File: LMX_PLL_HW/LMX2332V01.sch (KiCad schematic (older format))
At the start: 50 parts, among them J1 Conn_Coaxial, J2 Conn_01x04_Male, J3 Screw_Terminal_01x02, U1 Z-CommV440, U2 LMX2332, U3 ToyocomTCXO, U4 TPS784-Q1, U5 TPS784-Q1

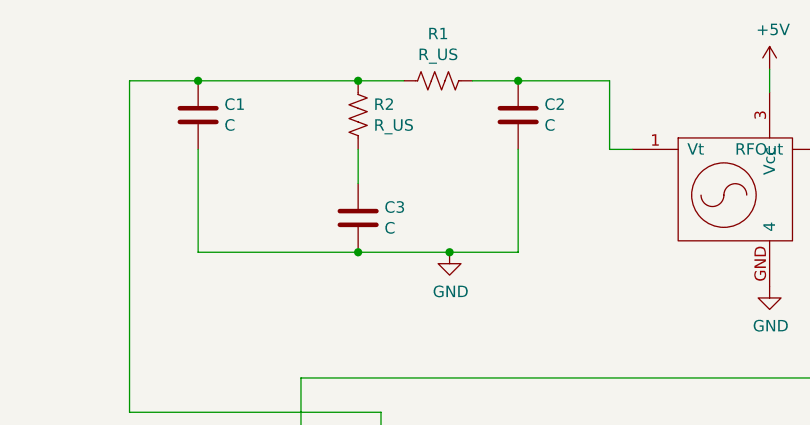
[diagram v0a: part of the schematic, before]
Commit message: Update 2021-07-05
Finished Schematic enough to get a first cut pulled into the layout.

Also finished PLL_Calculations.py enought to get loop filter component footprints nailed. Still needs more work, but ongoing. I'm using Spyder as a Python IDE.
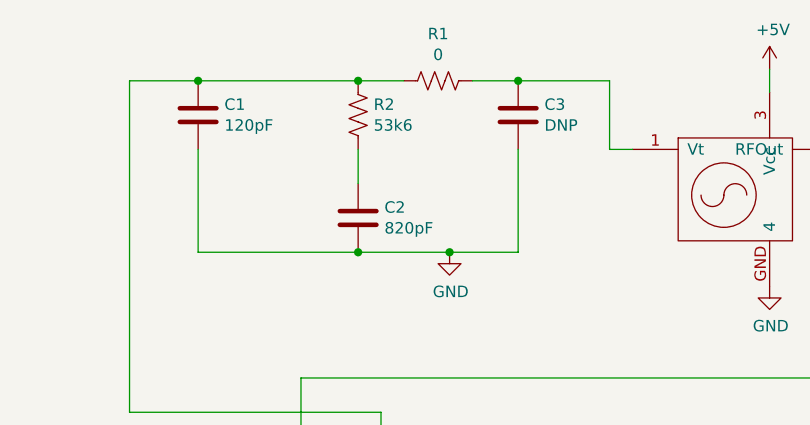
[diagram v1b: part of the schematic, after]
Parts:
- C1: value C -> 120pF; footprint (none) -> Capacitors_SMD:C_0805_HandSoldering
- C2: renamed from C3; value C -> 820pF; footprint (none) -> Capacitors_SMD:C_0805_HandSoldering
- C3: renamed from C2; value C -> DNP; footprint (none) -> Capacitors_SMD:C_0805_HandSoldering
- FB1: footprint (none) -> Capacitors_SMD:C_0805_HandSoldering
- J2: footprint (none) -> Connector_PinHeader_2.54mm:PinHeader_1x04_P2.54mm_Vertical
- J3: footprint (none) -> TerminalBlock_TE-Connectivity:TerminalBlock_TE_282834-2_1x02_P2.54mm_Horizontal
- R1: value R_US -> 0
- R2: value R_US -> 53k6
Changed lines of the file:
@@
 P 1950 1150
 F 0 "C1" H 2065 1196 50  0000 L CNN
-F 1 "C" H 2065 1105 50  0000 L CNN
-F 2 "" H 1988 1000 50  0001 C CNN
+F 1 "120pF" H 2065 1105 50  0000 L CNN
+F 2 "Capacitors_SMD:C_0805_HandSoldering" H 1988 1000 50  0001 C CNN
 F 3 "~" H 1950 1150 50  0001 C CNN
 	1    1950 1150
@@
 $EndComp
 $Comp
-L Device:C C3
+L Device:C C2
 U 1 1 60A5CF1C
 P 2650 1600
-F 0 "C3" H 2765 1646 50  0000 L CNN
-F 1 "C" H 2765 1555 50  0000 L CNN
-F 2 "" H 2688 1450 50  0001 C CNN
+F 0 "C2" H 2765 1646 50  0000 L CNN
+F 1 "820pF" H 2765 1555 50  0000 L CNN
+F 2 "Capacitors_SMD:C_0805_HandSoldering" H 2688 1450 50  0001 C CNN
 F 3 "~" H 2650 1600 50  0001 C CNN
 	1    2650 1600
@@
 $EndComp
 $Comp
-L Device:C C2
+L Device:C C3
 U 1 1 60A5D54A
 P 3350 1150
-F 0 "C2" H 3465 1196 50  0000 L CNN
-F 1 "C" H 3465 1105 50  0000 L CNN
-F 2 "" H 3388 1000 50  0001 C CNN
+F 0 "C3" H 3465 1196 50  0000 L CNN
+F 1 "DNP" H 3465 1105 50  0000 L CNN
+F 2 "Capacitors_SMD:C_0805_HandSoldering" H 3388 1000 50  0001 C CNN
 F 3 "~" H 3350 1150 50  0001 C CNN
 	1    3350 1150
@@
 P 2650 1150
 F 0 "R2" H 2718 1196 50  0000 L CNN
-F 1 "R_US" H 2718 1105 50  0000 L CNN
+F 1 "53k6" H 2718 1105 50  0000 L CNN
 F 2 "Resistors_SMD:R_0805_HandSoldering" V 2690 1140 50  0001 C CNN
 F 3 "~" H 2650 1150 50  0001 C CNN
@@
 P 3000 1000
 F 0 "R1" V 2795 1000 50  0000 C CNN
-F 1 "R_US" V 2886 1000 50  0000 C CNN
+F 1 "0" V 2886 1000 50  0000 C CNN
 F 2 "Resistors_SMD:R_0805_HandSoldering" V 3040 990 50  0001 C CNN
 F 3 "~" H 3000 1000 50  0001 C CNN
@@
 F 0 "J3" H 1118 9267 50  0000 C CNN
 F 1 "Screw_Terminal_01x02" H 1150 8850 50  0000 C CNN
-F 2 "" H 1200 9050 50  0001 C CNN
+F 2 "TerminalBlock_TE-Connectivity:TerminalBlock_TE_282834-2_1x02_P2.54mm_Horizontal" H 1200 9050 50  0001 C CNN
 F 3 "~" H 1200 9050 50  0001 C CNN
 	1    1200 9050
@@
 F 0 "FB1" V 1263 9050 50  0000 C CNN
 F 1 "Ferrite_Bead_Small" V 1350 9350 50  0000 C CNN
-F 2 "" V 1430 9050 50  0001 C CNN
+F 2 "Capacitors_SMD:C_0805_HandSoldering" V 1430 9050 50  0001 C CNN
 F 3 "~" H 1500 9050 50  0001 C CNN
 	1    1500 9050
@@
 F 0 "J2" H 7658 5531 50  0000 C CNN
 F 1 "Conn_01x04_Male" H 7658 5440 50  0000 C CNN
-F 2 "" H 7550 5250 50  0001 C CNN
+F 2 "Connector_PinHeader_2.54mm:PinHeader_1x04_P2.54mm_Vertical" H 7550 5250 50  0001 C CNN
 F 3 "~" H 7550 5250 50  0001 C CNN
 	1    7550 5250

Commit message: PCB Layout Updates. Not completed yet
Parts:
- removed J1: Conn_Coaxial, symbol Connector:Conn_Coaxial
- added H1, H2, H3, H4: MountingHole, Mounting_Holes:MountingHole_3.2mm_M3_DIN965_Pad, symbol Mechanical:MountingHole
- added J1: 142-0701-201, LMX_PLL_HW:JOHNSON_142-0701-201, symbol DB_KiCad:142-0701-201
- added R19, R20: 0, Resistors_SMD:R_0805_HandSoldering, symbol Device:R_US
- D1, D2: footprint LED_SMD:LED_LiteOn_LTST-S326 -> LED_SMD:LED_0805_2012Metric
- J2: footprint Connector_PinHeader_2.54mm:PinHeader_1x04_P2.54mm_Vertical -> Connector_JST:JST_SH_SM04B-SRSS-TB_1x04-1MP_P1.00mm_Horizontal
- U1: symbol DB_KiCad:Z-CommV440 -> LMX2332V01-rescue:Z-CommV440-DB_KiCad
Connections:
- net +3V0: now also R20.2; no longer C10.1, C8.1, D2.2 (A), R10.1, U5.5 (VOUT)
- net +5V: now also R19.2; no longer C6.1, C7.1, D1.2 (A), R9.1, U4.5 (VOUT)
- net GND: now also J1.2, J1.3, J1.4, J1.5
- net at R4.1: now also J1.1
- new net: C6.1, C7.1, D1.2 (A), R19.1, R9.1, U4.5 (VOUT)
- new net: C10.1, C8.1, D2.2 (A), R10.1, R20.1, U5.5 (VOUT)
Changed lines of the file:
@@
 $EndDescr
 $Comp
-L DB_KiCad:Z-CommV440 U1
+L LMX2332V01-rescue:Z-CommV440-DB_KiCad U1
 U 1 1 60A5B98C
 P 4300 1450
@@
 $EndComp
 $Comp
-L Connector:Conn_Coaxial J1
-U 1 1 60A5F56F
-P 6700 1300
-F 0 "J1" H 6800 1275 50  0000 L CNN
-F 1 "Conn_Coaxial" H 6800 1184 50  0000 L CNN
-F 2 "" H 6700 1300 50  0001 C CNN
-F 3 " ~" H 6700 1300 50  0001 C CNN
-	1    6700 1300
-	1    0    0    -1
-$EndComp
-$Comp
 L Device:R_US R5
 U 1 1 60A60489
@@
 F 0 "J2" H 7658 5531 50  0000 C CNN
 F 1 "Conn_01x04_Male" H 7658 5440 50  0000 C CNN
-F 2 "Connector_PinHeader_2.54mm:PinHeader_1x04_P2.54mm_Vertical" H 7550 5250 50  0001 C CNN
+F 2 "Connector_JST:JST_SH_SM04B-SRSS-TB_1x04-1MP_P1.00mm_Horizontal" H 7550 5250 50  0001 C CNN
 F 3 "~" H 7550 5250 50  0001 C CNN
 	1    7550 5250
@@
 L power:+5V #PWR0104
 U 1 1 60BCE0DC
-P 2950 7000
-F 0 "#PWR0104" H 2950 6850 50  0001 C CNN
-F 1 "+5V" H 2965 7173 50  0000 C CNN
-F 2 "" H 2950 7000 50  0001 C CNN
-F 3 "" H 2950 7000 50  0001 C CNN
-	1    2950 7000
+P 3250 6650
+F 0 "#PWR0104" H 3250 6500 50  0001 C CNN
+F 1 "+5V" H 3265 6823 50  0000 C CNN
+F 2 "" H 3250 6650 50  0001 C CNN
+F 3 "" H 3250 6650 50  0001 C CNN
+	1    3250 6650
 	1    0    0    -1
 $EndComp
@@
 L power:+3V0 #PWR0109
 U 1 1 60BF6B29
-P 5600 7100
-F 0 "#PWR0109" H 5600 6950 50  0001 C CNN
-F 1 "+3V0" H 5615 7273 50  0000 C CNN
-F 2 "" H 5600 7100 50  0001 C CNN
-F 3 "" H 5600 7100 50  0001 C CNN
-	1    5600 7100
+P 5900 6800
+F 0 "#PWR0109" H 5900 6650 50  0001 C CNN
+F 1 "+3V0" H 5915 6973 50  0000 C CNN
+F 2 "" H 5900 6800 50  0001 C CNN
+F 3 "" H 5900 6800 50  0001 C CNN
+	1    5900 6800
 	1    0    0    -1
 $EndComp
@@
 L power:GND #PWR0112
 U 1 1 60C10F3C
-P 6700 1500
-F 0 "#PWR0112" H 6700 1250 50  0001 C CNN
-F 1 "GND" H 6705 1327 50  0000 C CNN
-F 2 "" H 6700 1500 50  0001 C CNN
-F 3 "" H 6700 1500 50  0001 C CNN
-	1    6700 1500
+P 6450 1500
+F 0 "#PWR0112" H 6450 1250 50  0001 C CNN
+F 1 "GND" H 6455 1327 50  0000 C CNN
+F 2 "" H 6450 1500 50  0001 C CNN
+F 3 "" H 6450 1500 50  0001 C CNN
+	1    6450 1500
 	1    0    0    -1
 $EndComp
@@
 F 0 "D1" V 3339 7082 50  0000 R CNN
 F 1 "LED" V 3248 7082 50  0000 R CNN
-F 2 "LED_SMD:LED_LiteOn_LTST-S326" H 3300 7200 50  0001 C CNN
+F 2 "LED_SMD:LED_0805_2012Metric" H 3300 7200 50  0001 C CNN
 F 3 "~" H 3300 7200 50  0001 C CNN
 	1    3300 7200
@@
 F 0 "D2" V 6139 7232 50  0000 R CNN
 F 1 "LED" V 6048 7232 50  0000 R CNN
-F 2 "LED_SMD:LED_LiteOn_LTST-S326" H 6100 7350 50  0001 C CNN
+F 2 "LED_SMD:LED_0805_2012Metric" H 6100 7350 50  0001 C CNN
 F 3 "~" H 6100 7350 50  0001 C CNN
 	1    6100 7350
@@
 $EndComp
 Wire Wire Line
-	2950 7000 3300 7000
-Wire Wire Line
 	3300 7000 3300 7050
 Wire Wire Line
@@
 Connection ~ 2950 7900
 Wire Wire Line
-	5600 7100 6100 7100
+	5600 7100 5900 7100
 Wire Wire Line
 	6100 7100 6100 7200
@@
 Wire Wire Line
 	4500 5550 4500 5750
+$Comp
+L DB_KiCad:142-0701-201 J1
+U 1 1 60F3E1CE
+P 6600 1400
+F 0 "J1" H 6440 1486 50  0000 R CNN
+F 1 "142-0701-201" H 6440 1395 50  0000 R CNN
+F 2 "LMX_PLL_HW:JOHNSON_142-0701-201" H 6600 1400 50  0001 L BNN
+F 3 "" H 6600 1400 50  0001 L BNN
+F 4 "Manufacturer Recommendation" H 6600 1400 50  0001 L BNN "STANDARD"
+F 5 "Johnson" H 6600 1400 50  0001 L BNN "MANUFACTURER"
+	1    6600 1400
+	-1   0    0    -1
+$EndComp
+Wire Wire Line
+	6500 1400 6500 1500
+Wire Wire Line
+	6500 1500 6450 1500
+$Comp
+L Device:R_US R19
+U 1 1 60F80BDD
+P 3250 6800
+F 0 "R19" V 3045 6800 50  0000 C CNN
+F 1 "0" V 3136 6800 50  0000 C CNN
+F 2 "Resistors_SMD:R_0805_HandSoldering" V 3290 6790 50  0001 C CNN
+F 3 "~" H 3250 6800 50  0001 C CNN
+	1    3250 6800
+	-1   0    0    1
+$EndComp
+Wire Wire Line
+	3250 6950 3250 7000
+Wire Wire Line
+	2950 7000 3250 7000
+Connection ~ 3250 7000
+Wire Wire Line
+	3250 7000 3300 7000
+$Comp
+L Device:R_US R20
+U 1 1 60F94213
+P 5900 6950
+F 0 "R20" V 5695 6950 50  0000 C CNN
+F 1 "0" V 5786 6950 50  0000 C CNN
+F 2 "Resistors_SMD:R_0805_HandSoldering" V 5940 6940 50  0001 C CNN
+F 3 "~" H 5900 6950 50  0001 C CNN
+	1    5900 6950
+	-1   0    0    1
+$EndComp
+Connection ~ 5900 7100
+Wire Wire Line
+	5900 7100 6100 7100
+$Comp
+L Mechanical:MountingHole H1
+U 1 1 611BBB9F
+P 6600 7250
+F 0 "H1" H 6700 7296 50  0000 L CNN
+F 1 "MountingHole" H 6700 7205 50  0000 L CNN
+F 2 "Mounting_Holes:MountingHole_3.2mm_M3_DIN965_Pad" H 6600 7250 50  0001 C CNN
+F 3 "~" H 6600 7250 50  0001 C CNN
+	1    6600 7250
+	1    0    0    -1
+$EndComp
+$Comp
+L Mechanical:MountingHole H2
+U 1 1 611BC72D
+P 6600 7500
+F 0 "H2" H 6700 7546 50  0000 L CNN
+F 1 "MountingHole" H 6700 7455 50  0000 L CNN
+F 2 "Mounting_Holes:MountingHole_3.2mm_M3_DIN965_Pad" H 6600 7500 50  0001 C CNN
+F 3 "~" H 6600 7500 50  0001 C CNN
+	1    6600 7500
+	1    0    0    -1
+$EndComp
+$Comp
+L Mechanical:MountingHole H3
+U 1 1 611BCE2A
+P 6600 7750
+F 0 "H3" H 6700 7796 50  0000 L CNN
+F 1 "MountingHole" H 6700 7705 50  0000 L CNN
+F 2 "Mounting_Holes:MountingHole_3.2mm_M3_DIN965_Pad" H 6600 7750 50  0001 C CNN
+F 3 "~" H 6600 7750 50  0001 C CNN
+	1    6600 7750
+	1    0    0    -1
+$EndComp
+$Comp
+L Mechanical:MountingHole H4
+U 1 1 611BD6CA
+P 6600 8000
+F 0 "H4" H 6700 8046 50  0000 L CNN
+F 1 "MountingHole" H 6700 7955 50  0000 L CNN
+F 2 "Mounting_Holes:MountingHole_3.2mm_M3_DIN965_Pad" H 6600 8000 50  0001 C CNN
+F 3 "~" H 6600 8000 50  0001 C CNN
+	1    6600 8000
+	1    0    0    -1
+$EndComp
 $EndSCHEMATC
